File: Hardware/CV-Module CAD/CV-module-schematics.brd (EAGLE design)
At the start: 160 x 100 mm, 97 parts, among them IC2 LM358D, IC3 LM358D, IC4 LM358D, IC5 LM358D, U1 AD5611BKSZ, U2 AD5611BKSZ, U3 AD5611BKSZ, U4 AD5611BKSZ, U5 AD5611BKSZ, U6 AD5611BKSZ, U7 AD5611BKSZ, U8 AD5611BKSZ

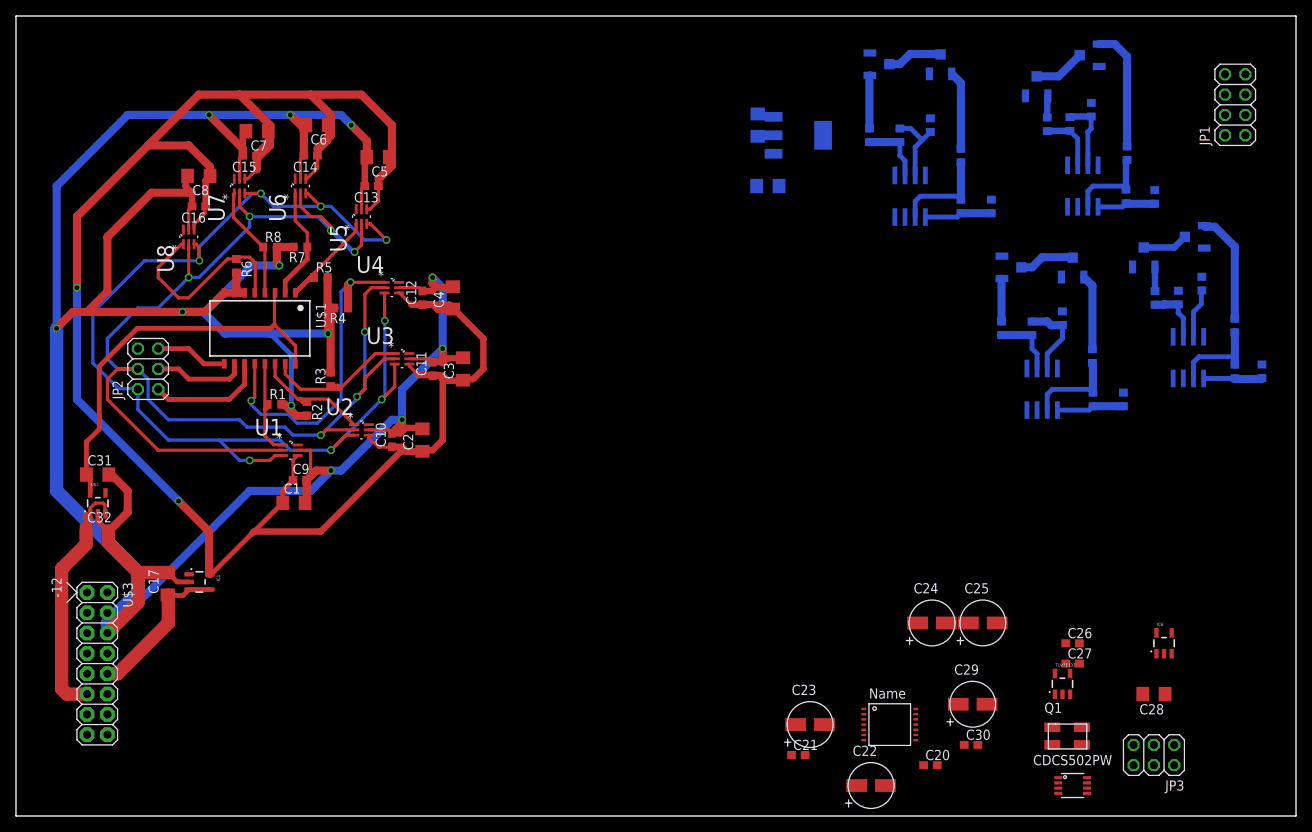
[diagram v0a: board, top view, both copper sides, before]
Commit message: Schemas and layout updated
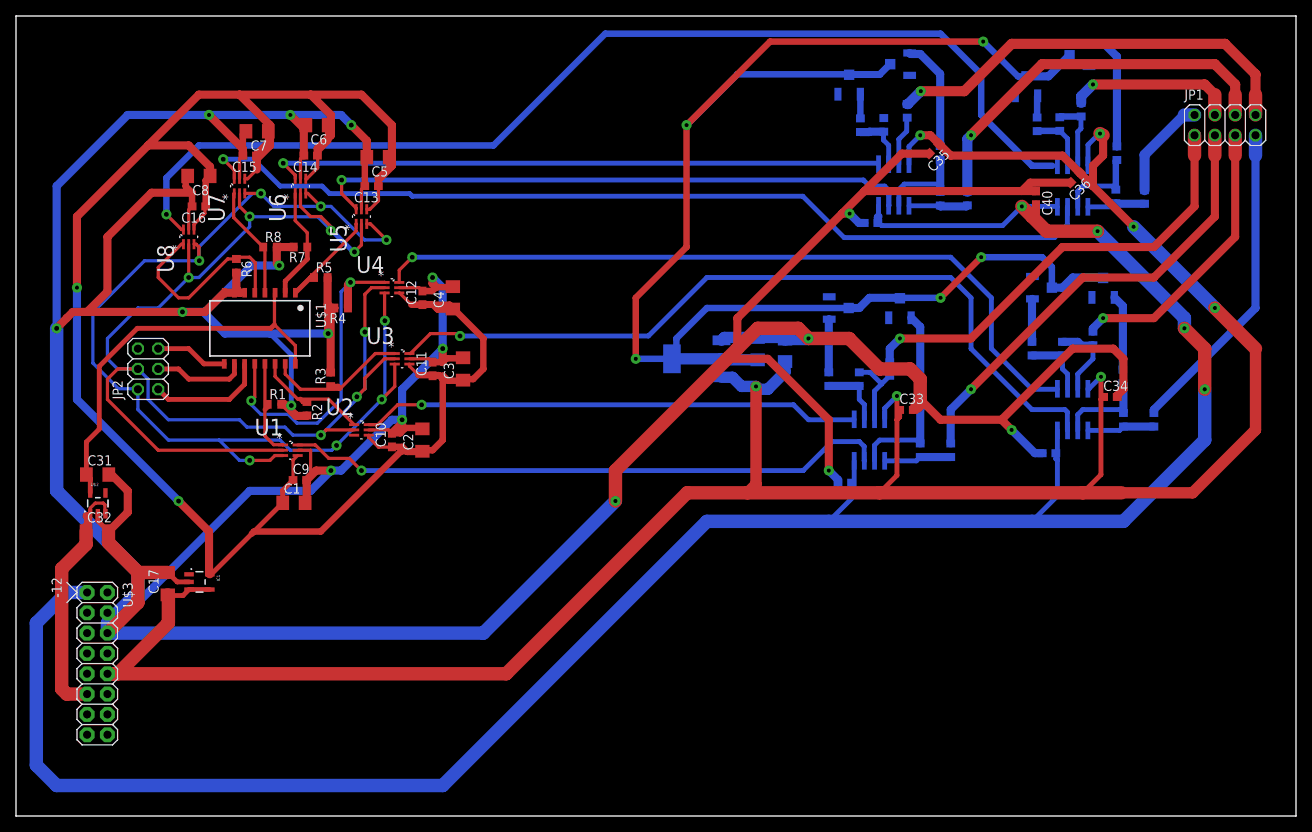
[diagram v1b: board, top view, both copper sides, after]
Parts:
- removed C20, C21, C26, C27, C30: 0.1uF, rcl:C0603
- removed C22, C23, C29: 10uF, rcl:RADIALCAN4MM
- removed C24, C25: 1uF, rcl:RADIALCAN4MM
- removed C28: (no value), rcl:C1206
- removed CDCS502PW: CDCS502, components:SSOP-8
- removed IC6: (no value), SparkFun-PowerIC:SOT23-5
- removed JP3: (no value), pinhead:2X03
- removed PCM1808: PCM1808PW, Pekkas_libraries:R-PDSO-G14
- removed Q1: (no value), Pekkas_libraries:5X3CRYSTAL
- removed TLV71333: TVL713, Pekkas_libraries:SOT23-5
- added C33, C34, C35, C36, C37, C38, C39, C40: 0.1uF, resistor:C0603
- moved IC4 42.7 mm to (109.7, 78.9)
- moved R21 42.7 mm to (115.5, 77.2)
- moved R23 42.7 mm to (108.5, 86.4)
- moved R20 42.7 mm to (115.5, 82.9)
- moved R32 42.7 mm to (110.5, 94.0)
- moved R33 42.7 mm to (104.1, 91.4)
- moved R40 42.7 mm to (118.9, 77.2)
- moved R22 42.7 mm to (105.5, 86.3)
- moved R41 42.7 mm to (111.4, 88.1)
- moved R14 30.9 mm to (101.6, 54.6)
- moved R13 30.9 mm to (113.0, 45.7)
- moved R15 30.9 mm to (105.4, 54.6)
- moved R28 30.9 mm to (110.5, 63.5)
- moved R29 30.9 mm to (102.9, 63.5)
- moved R36 30.9 mm to (116.8, 45.7)
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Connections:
- removed net 3V3: C21.1, C23.1, C26.1, CDCS502PW.7, PCM1808.4, TLV71333.5
- removed net 5VCC: C20.1, C22.1, IC6.5, PCM1808.3
- removed net AGND: C20.2, C22.2
- removed net N$28: C25.1, PCM1808.13
- removed net N$29: CDCS502PW.1, Q1.1
- removed net N$3: C24.1, PCM1808.14
- removed net N$30: CDCS502PW.8, Q1.3
- removed net N$31: C29.1, C30.1
- removed net N$32: CDCS502PW.6, PCM1808.6
- removed net N$33: JP3.1, PCM1808.7
- removed net N$34: JP3.2, PCM1808.9
- removed net N$35: JP3.3, PCM1808.8
- net +12VDC: now also C33.1, C34.1, C35.1, C36.1; no longer C28.1, IC6.3, IC6.4
- net -12VDC: now also C37.2, C38.2, C39.2, C40.2
- net 5VCON: no longer C27.1, TLV71333.1, TLV71333.3
- net CV1: now also R37.2; no longer R36.2
- net CV2: now also R36.2; no longer R37.2
- net CV3: now also R39.2
- net CV4: no longer R39.2
- net CV5: now also R42.2; no longer R40.2
- net CV6: now also R43.2; no longer R41.2
- net CV7: now also R40.2; no longer R42.2
- net CV8: now also R41.2; no longer R43.2
- net GND: now also C33.2, C34.2, C35.2, C36.2, C37.1, C38.1, C39.1, C40.1; no longer C21.2, C23.2, C26.2, C27.2, C28.2, C29.2, C30.2, CDCS502PW.2, CDCS502PW.3, CDCS502PW.4, CDCS502PW.5, IC6.2, JP3.4, PCM1808.10, PCM1808.11, PCM1808.12, PCM1808.2, PCM1808.5, TLV71333.2
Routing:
- net +12VDC: track 19.3 -> 315.4 mm, vias 0 -> 7
- net -12VDC: track 0.00 -> 285.0 mm, vias 0 -> 4
- net GND: track 407.4 -> 679.4 mm, vias 12 -> 17
- net +5V: track 26.1 -> 201.1 mm, vias 0 -> 5
- net VDAC8: track 0.00 -> 135.5 mm, vias 0 -> 1
- net VDAC7: track 0.00 -> 115.5 mm, vias 0 -> 1
- net VDAC3: track 0.00 -> 99.4 mm, vias 0 -> 1
- net VDAC4: track 0.00 -> 95.1 mm, vias 0 -> 1
- net VDAC6: track 0.00 -> 77.0 mm, vias 0 -> 1
- net VDAC1: track 0.00 -> 75.7 mm, vias 0 -> 1
- net VDAC5: track 0.00 -> 75.3 mm, vias 0 -> 1
- net VDAC2: track 0.00 -> 62.5 mm, vias 0 -> 1
- net CV2: track 0.00 -> 57.4 mm, vias 0 -> 1
- net CV1: track 0.00 -> 56.0 mm, vias 0 -> 1
- net CV8: track 0.00 -> 53.3 mm, vias 0 -> 1
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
